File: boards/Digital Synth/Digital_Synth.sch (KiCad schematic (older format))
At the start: 2 parts, among them U1 STM32F446RETx

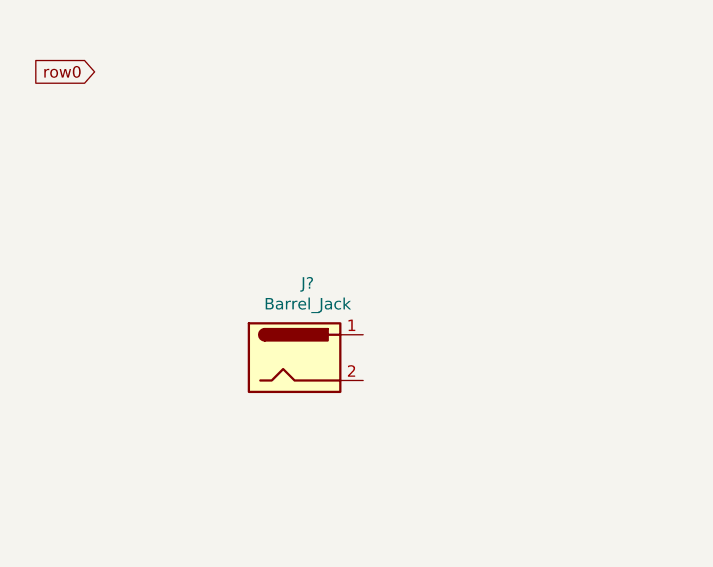
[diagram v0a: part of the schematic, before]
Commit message: progress on layout for DAC and MIDI
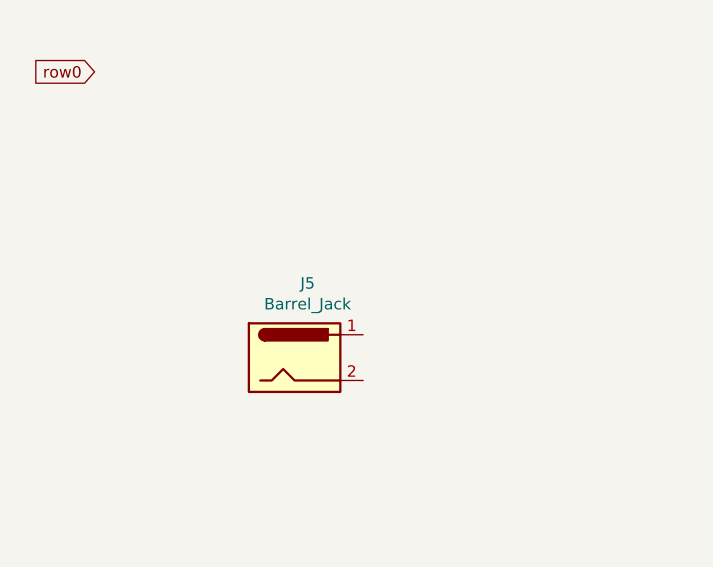
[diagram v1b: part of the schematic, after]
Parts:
- gave numbers to parts that had none: 1
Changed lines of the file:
@@
 $EndSheet
 $Comp
-L Connector:Barrel_Jack J?
+L Connector:Barrel_Jack J5
 U 1 1 6226EE84
 P 2375 3675
-F 0 "J?" H 2432 4000 50  0000 C CNN
+F 0 "J5" H 2432 4000 50  0000 C CNN
 F 1 "Barrel_Jack" H 2432 3909 50  0000 C CNN
 F 2 "" H 2425 3635 50  0001 C CNN

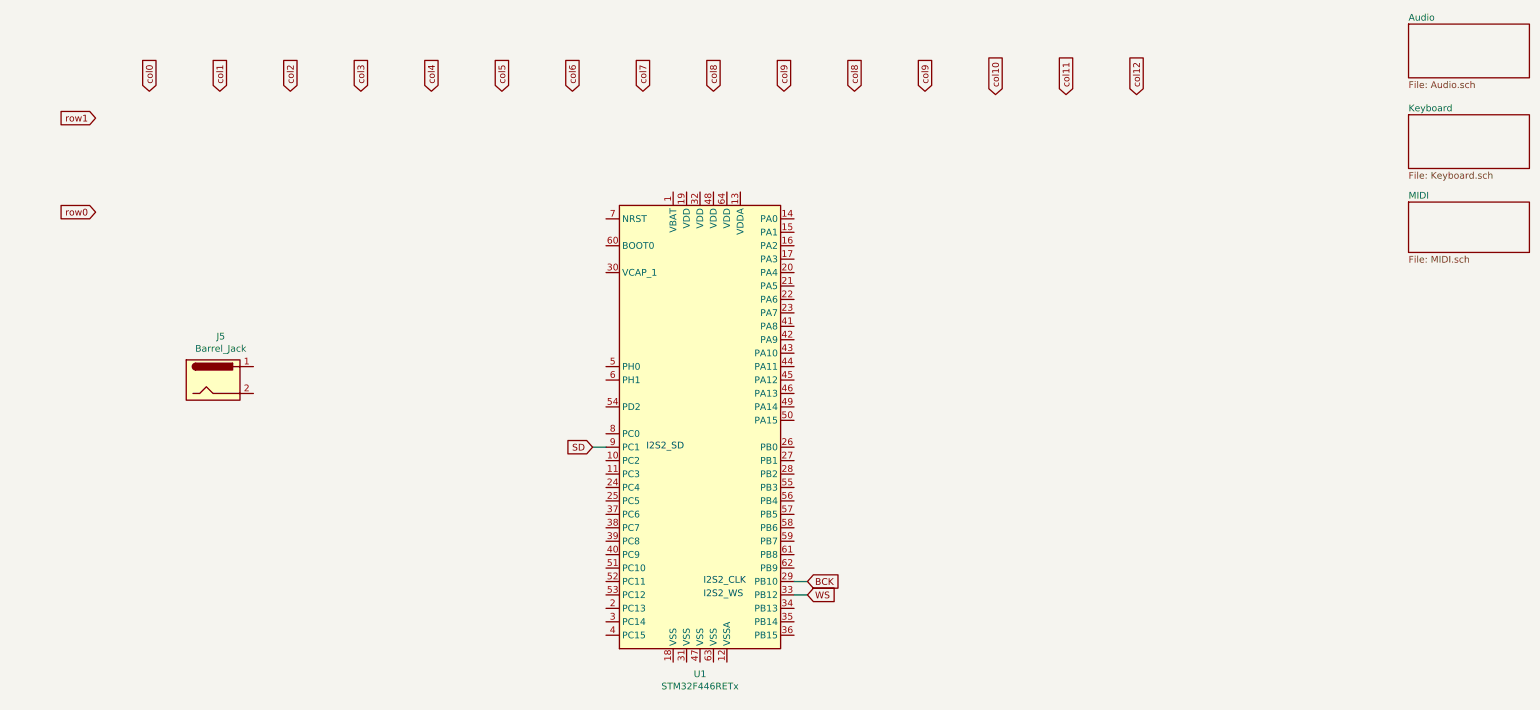
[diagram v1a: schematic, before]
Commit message: laid out keyboard
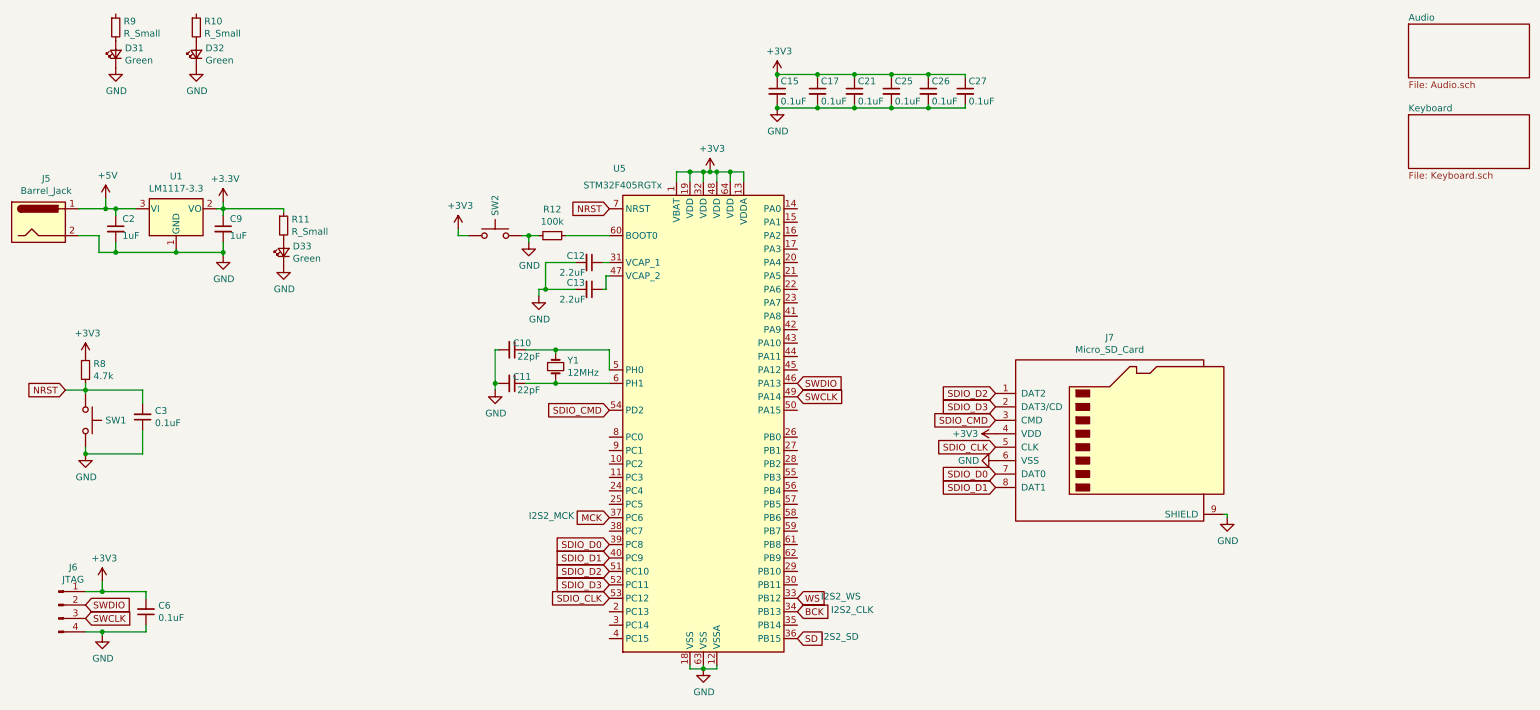
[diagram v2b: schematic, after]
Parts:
- removed U1: STM32F446RETx, Package_QFP:LQFP-64_10x10mm_P0.5mm, symbol MCU_ST_STM32F4:STM32F446RETx
- added C10, C11: 22pF, symbol device:C_Small
- added C12, C13: 2.2uF, symbol device:C_Small
- added C15, C17, C21, C25, C26, C27, C3, C6: 0.1uF, Capacitor_SMD:C_0603_1608Metric_Pad1.05x0.95mm_HandSolder, symbol device:C_Small
- added C2, C9: 1uF, symbol device:C_Small
- added D31, D32, D33: Green, symbol device:LED_Small
- added J6: JTAG, symbol Connector:Conn_01x04_Male
- added J7: Micro_SD_Card, symbol Connector:Micro_SD_Card
- added R10, R11, R9: R_Small, symbol device:R_Small
- added R12: 100k, Resistor_SMD:R_0805_2012Metric_Pad1.15x1.40mm_HandSolder, symbol device:R_Small
- added R8: 4.7k, Resistor_SMD:R_0805_2012Metric_Pad1.15x1.40mm_HandSolder, symbol device:R_Small
- added SW1, SW2: SW_Push, symbol Switch:SW_Push
- added U1: LM1117-3.3, symbol Regulator_Linear:LM1117-3.3
- added U5: STM32F405RGTx, Package_QFP:LQFP-64_10x10mm_P0.5mm, symbol MCU_ST_STM32F4:STM32F405RGTx
- added Y1: 12MHz, symbol device:Crystal_Small
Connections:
- net BCK: now also U5.34 (PB13)
- net SD: now also U5.36 (PB15)
- net WS: now also U5.33 (PB12)
- net +5V: now reaches J5.1
- net +5V: now also C2.1, U1.3 (VI)
- net GND: now reaches J5.2
- net GND: now also C10.2, C11.2, C12.2, C13.2, C15.2, C17.2, C2.2, C21.2, C25.2, C26.2, C27.2, C3.1, C6.1, C9.2, D31.1 (K), D32.1 (K), D33.1 (K), J6.4 (Pin_4), J7.6 (VSS), J7.9 (SHIELD), R12.2, SW1.2, SW2.2, U1.1 (GND), U5.12 (VSSA), U5.18 (VSS), U5.63 (VSS)
- new net: C12.1, U5.31 (VCAP_1)
- new net: C13.1, U5.47 (VCAP_2)
- new net: C10.1, U5.5 (PH0), Y1.1
- new net: C11.1, U5.6 (PH1), Y1.2
- new net: R12.1, U5.60 (BOOT0)
- new net: D33.2 (A), R11.2
- new net: D31.2 (A), R9.2
- new net: D32.2 (A), R10.2
- new net +3V3: C15.1, C17.1, C21.1, C25.1, C26.1, C27.1, C6.2, C9.1, J6.1 (Pin_1), J7.4 (VDD), R11.1, R8.1, SW2.1, U1.2 (VO), U5.1 (VBAT), U5.13 (VDDA), U5.19 (VDD), U5.32 (VDD), U5.48 (VDD), U5.64 (VDD)
- new net MCK: U5.37 (PC6)
- new net NRST: C3.2, R8.2, SW1.1, U5.7 (NRST)
- new net SDIO_CLK: J7.5 (CLK), U5.53 (PC12)
- new net SDIO_CMD: J7.3 (CMD), U5.54 (PD2)
- new net SDIO_D0: J7.7 (DAT0), U5.39 (PC8)
- new net SDIO_D1: J7.8 (DAT1), U5.40 (PC9)
- new net SDIO_D2: J7.1 (DAT2), U5.51 (PC10)
- new net SDIO_D3: J7.2 (DAT3/CD), U5.52 (PC11)
- new net SWCLK: J6.3 (Pin_3), U5.49 (PA14)
- new net SWDIO: J6.2 (Pin_2), U5.46 (PA13)
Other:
- note added: "I2S2_MCK"
- moved on the sheet: J5
